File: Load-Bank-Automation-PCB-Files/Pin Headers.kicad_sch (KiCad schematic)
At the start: 23 parts, among them J10 Conn_01x04_Pin, J11 Conn_01x04_Pin, J12 Conn_01x04_Pin, J13 Conn_01x04_Pin, J14 Conn_01x04_Pin, J15 Conn_01x04_Pin, J16 Conn_01x04_Pin, J17 Conn_01x04_Pin, J18 Conn_01x04_Pin, J19 Conn_01x04_Pin, J20 Conn_01x04_Pin, J21 Conn_01x04_Pin, J22 Conn_01x04_Pin, J23 Conn_01x04_Pin, J4 Conn_01x04_Pin, J5 Conn_01x04_Pin, J6 Conn_01x04_Pin, J7 Conn_01x04_Pin, J8 Conn_01x04_Pin, J9 Conn_01x04_Pin, SW2 RESET, U9 STM32G491VETx

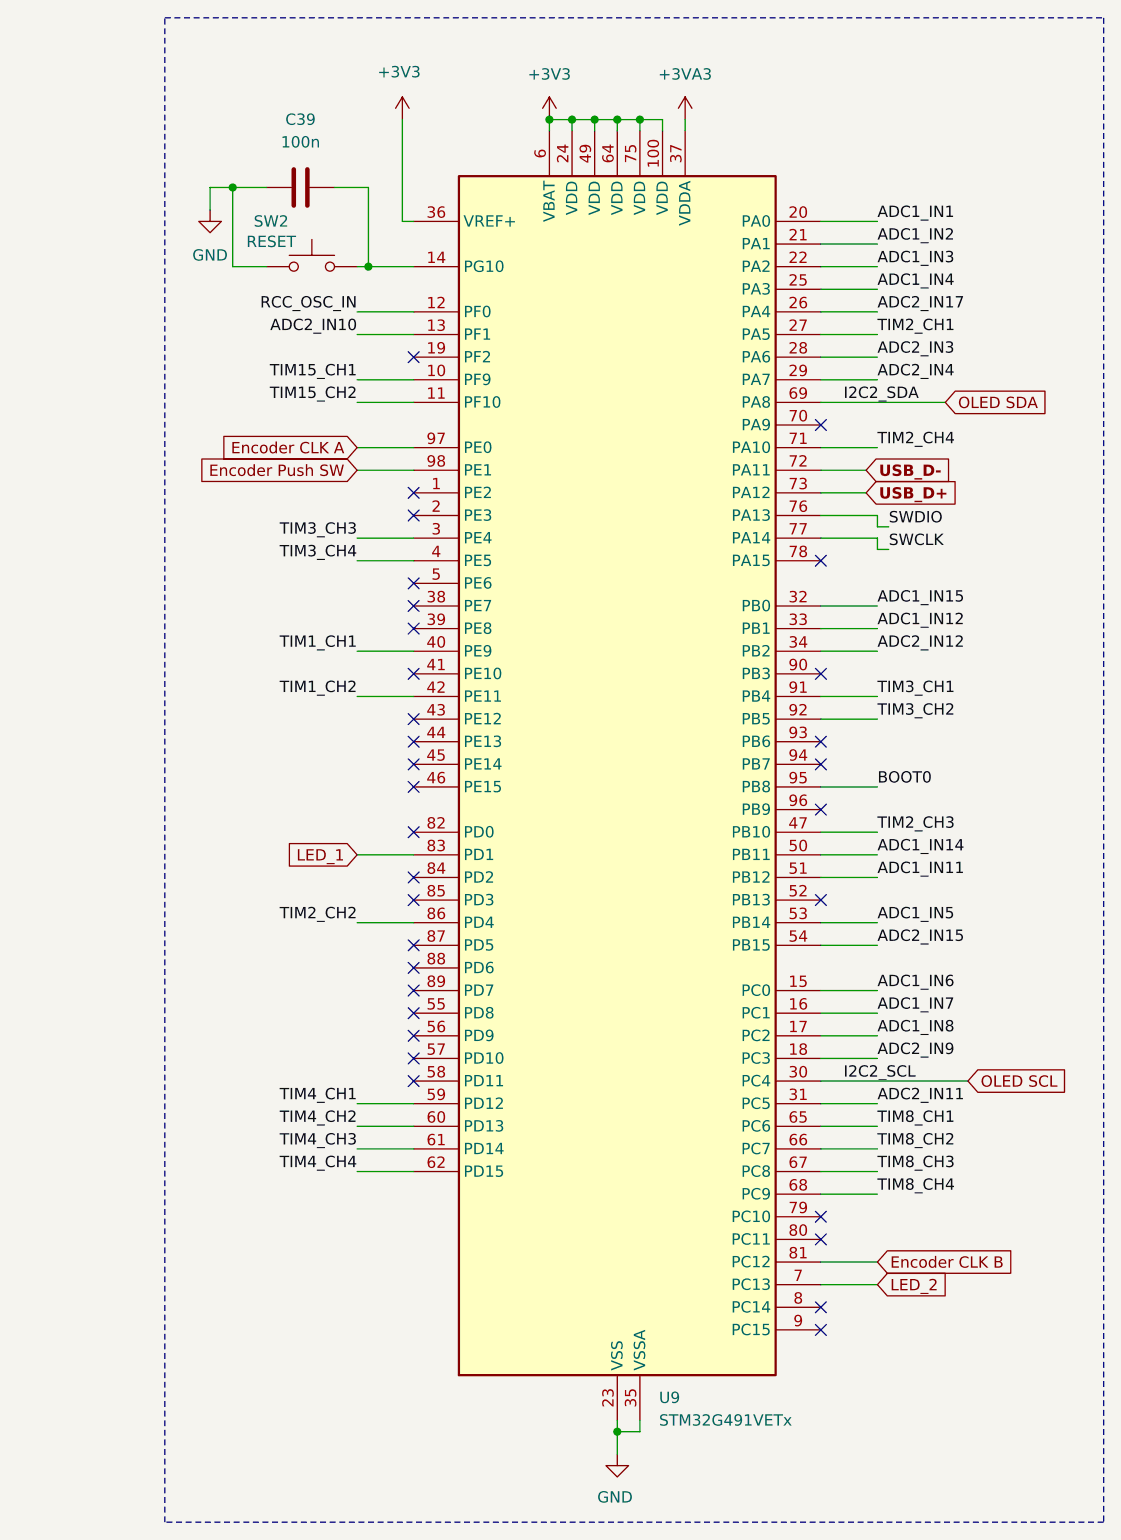
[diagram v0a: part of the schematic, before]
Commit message: Added potentiometer to buck converter and New schematic for MOSFET boards
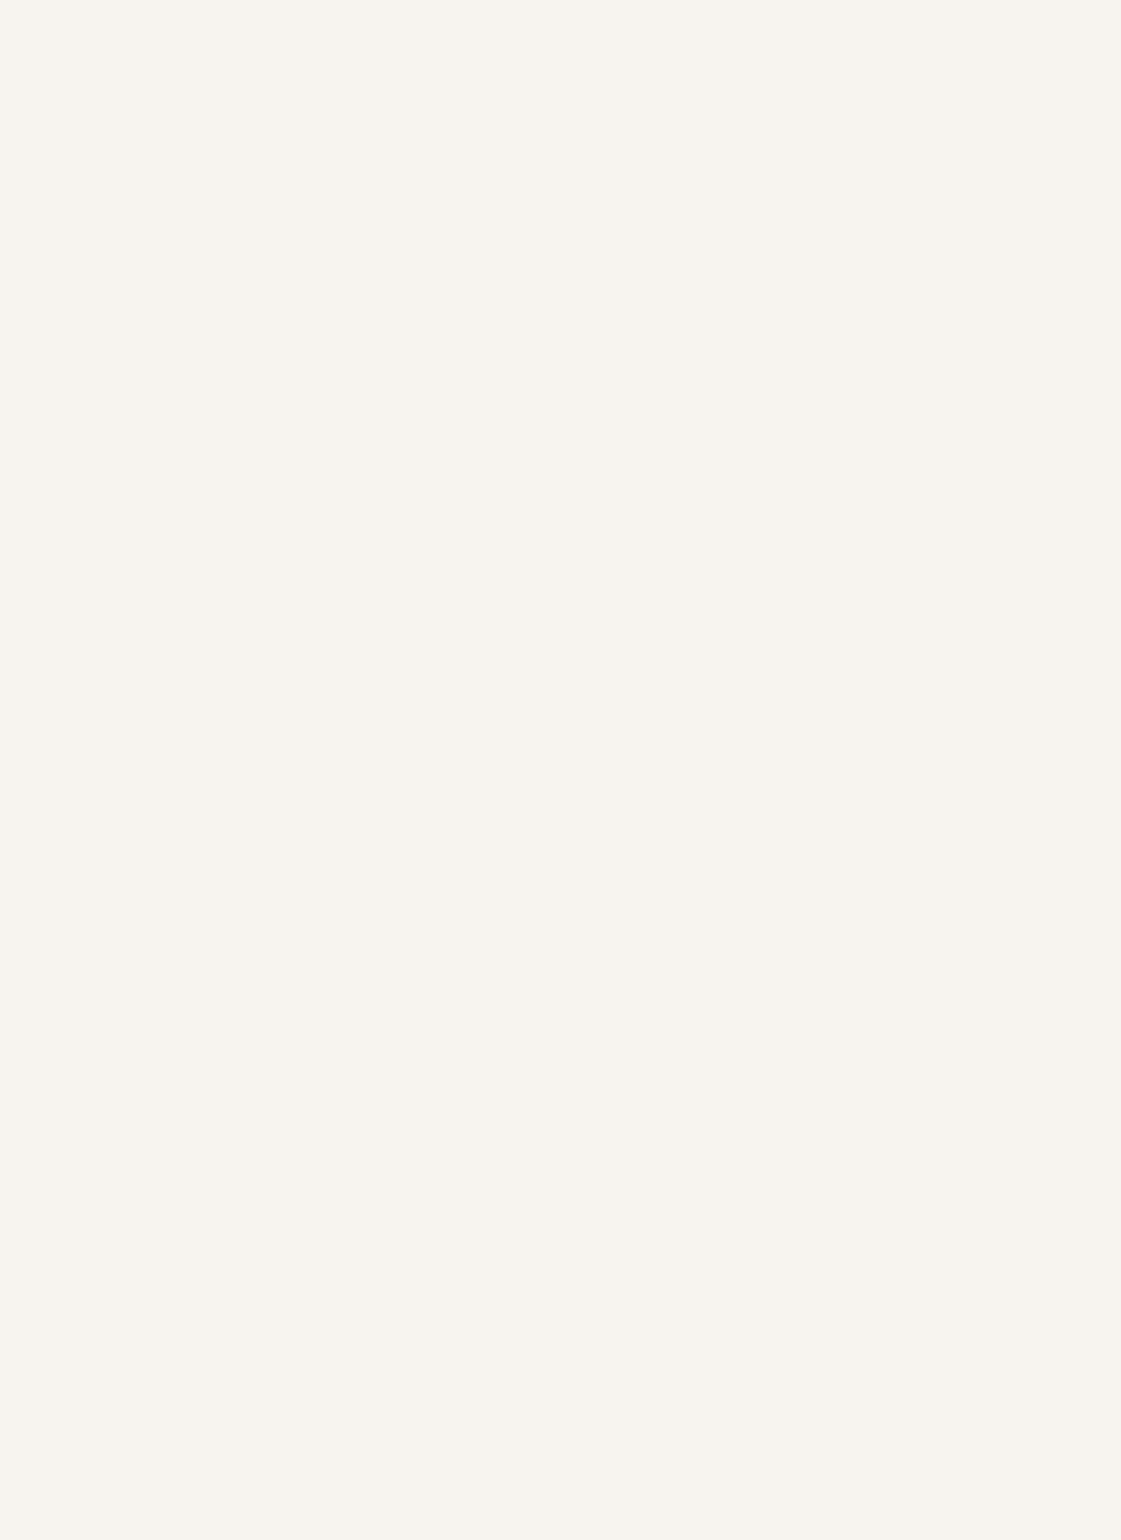
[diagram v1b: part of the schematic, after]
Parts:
- removed C39: 100n, symbol Device:C
- removed SW2: RESET, symbol Switch:SW_Push
- removed U9: STM32G491VETx, Package_QFP:LQFP-100_14x14mm_P0.5mm, symbol MCU_ST_STM32G4:STM32G491VETx
- J10, J11, J12, J13, J14, J15, J16, J17, J18, J19, J20, J21, J22, J23, J4, J5, J6, J7, J8, J9: footprint (none) -> Connector_PinHeader_2.54mm:PinHeader_1x04_P2.54mm_Vertical
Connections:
- no-connect marks 32 -> 0

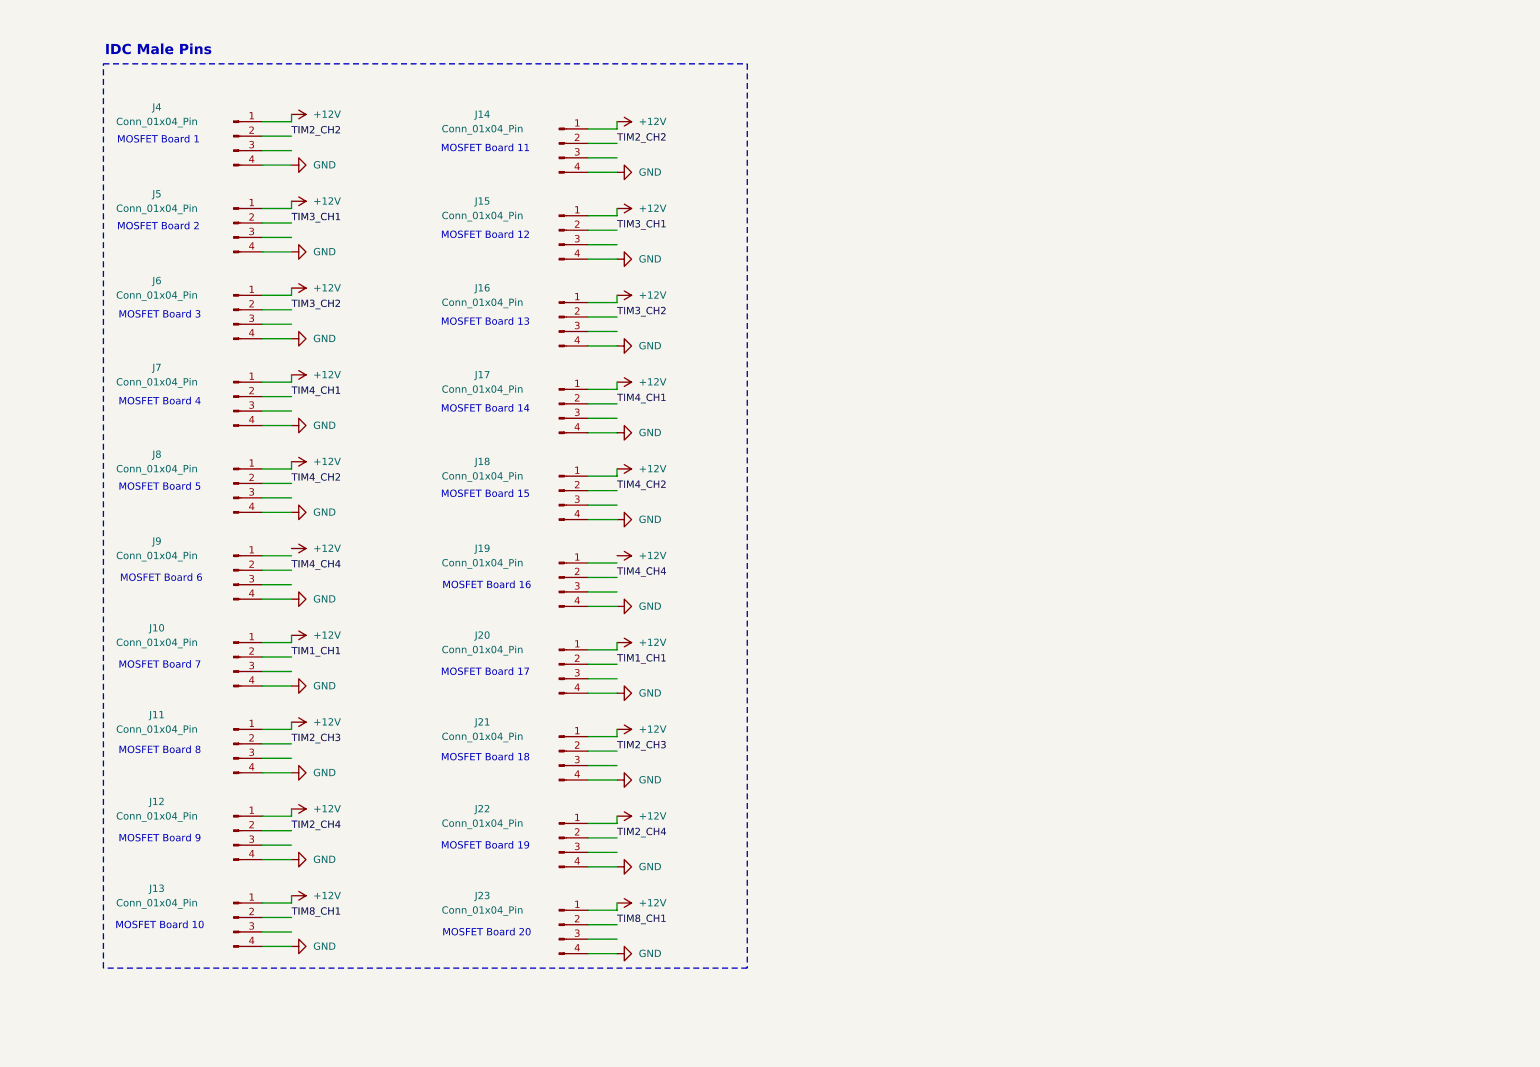
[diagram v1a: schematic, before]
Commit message: Comlpeted Schematic(needs some small component values only)
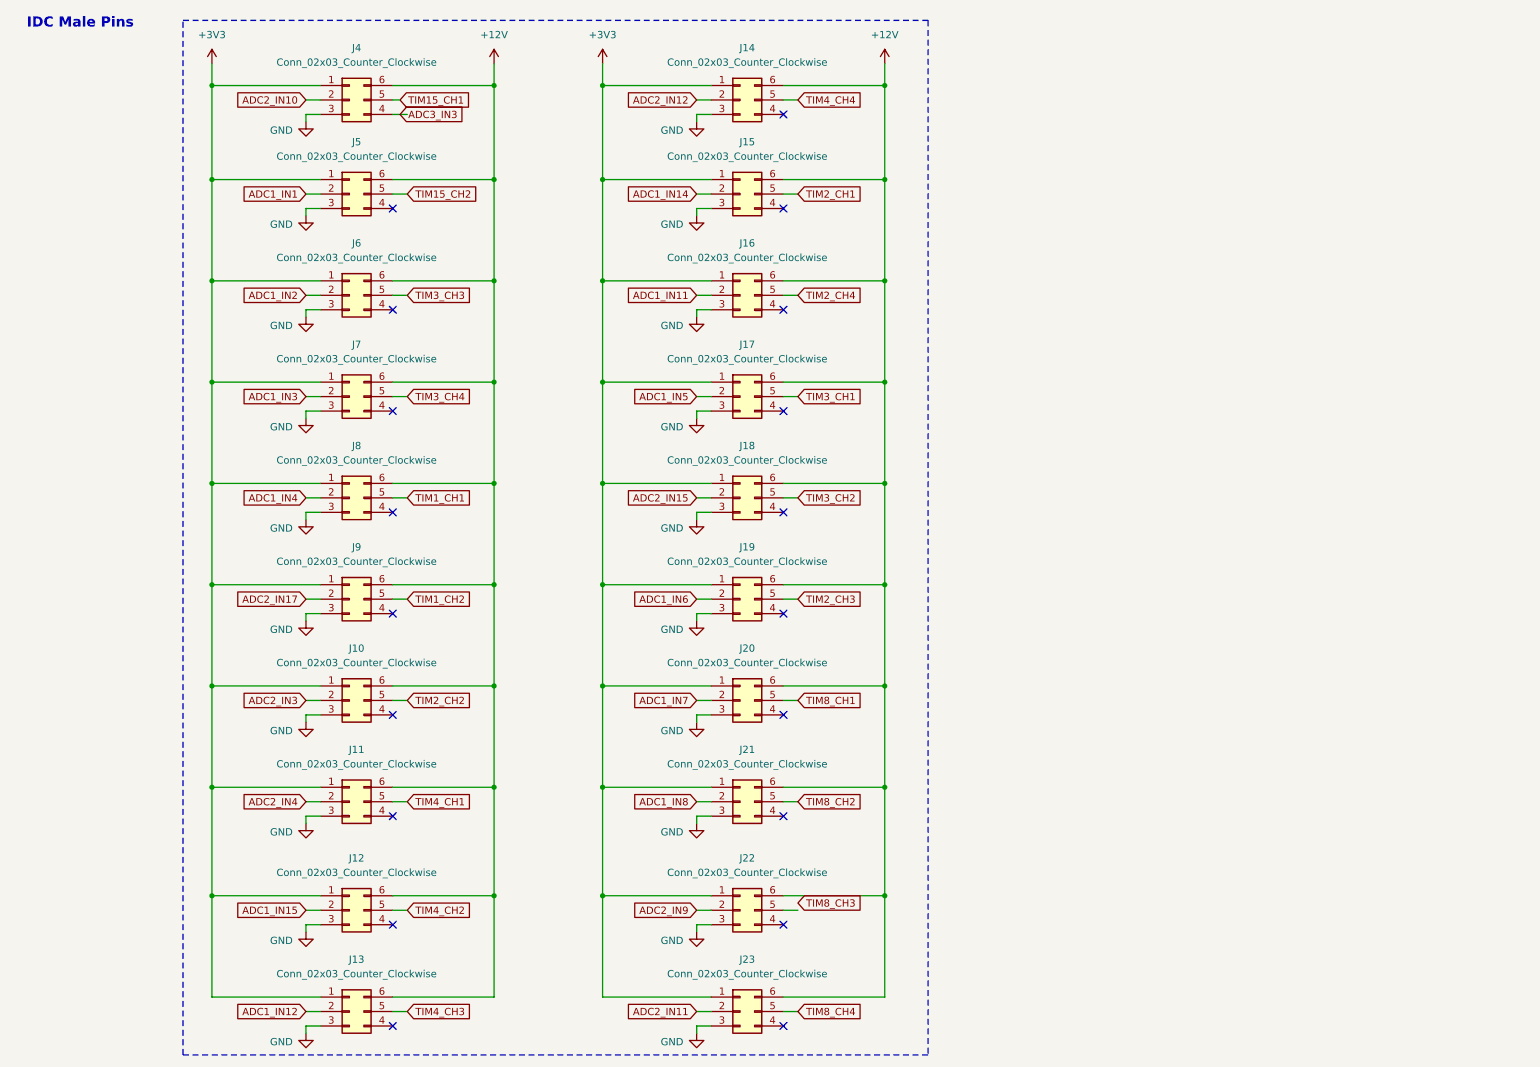
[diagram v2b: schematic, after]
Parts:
- removed J10, J11, J12, J13, J14, J15, J16, J17, J18, J19, J20, J21, J22, J23, J4, J5, J6, J7, J8, J9: Conn_01x04_Pin, Connector_PinHeader_2.54mm:PinHeader_1x04_P2.54mm_Vertical, symbol Connector:Conn_01x04_Pin
- added J10, J11, J12, J13, J14, J15, J16, J17, J18, J19, J20, J21, J22, J23, J4, J5, J6, J7, J8, J9: Conn_02x03_Counter_Clockwise, Connector_IDC:IDC-Header_2x03_P2.54mm_Vertical, symbol Connector_Generic:Conn_02x03_Counter_Clockwise
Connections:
- net +12V: now also J10.6 (Pin_6), J11.6 (Pin_6), J12.6 (Pin_6), J13.6 (Pin_6), J14.6 (Pin_6), J15.6 (Pin_6), J16.6 (Pin_6), J17.6 (Pin_6), J18.6 (Pin_6), J19.6 (Pin_6), J20.6 (Pin_6), J21.6 (Pin_6), J22.6 (Pin_6), J23.6 (Pin_6), J4.6 (Pin_6), J5.6 (Pin_6), J6.6 (Pin_6), J7.6 (Pin_6), J8.6 (Pin_6), J9.6 (Pin_6)
- net GND: now also J10.3 (Pin_3), J11.3 (Pin_3), J12.3 (Pin_3), J13.3 (Pin_3), J14.3 (Pin_3), J15.3 (Pin_3), J16.3 (Pin_3), J17.3 (Pin_3), J18.3 (Pin_3), J19.3 (Pin_3), J20.3 (Pin_3), J21.3 (Pin_3), J22.3 (Pin_3), J23.3 (Pin_3), J4.3 (Pin_3), J5.3 (Pin_3), J6.3 (Pin_3), J7.3 (Pin_3), J8.3 (Pin_3), J9.3 (Pin_3)
- net TIM1_CH1: now also J8.5 (Pin_5)
- net TIM2_CH2: now also J10.5 (Pin_5)
- net TIM2_CH3: now also J19.5 (Pin_5)
- net TIM2_CH4: now also J16.5 (Pin_5)
- net TIM3_CH1: now also J17.5 (Pin_5)
- net TIM3_CH2: now also J18.5 (Pin_5)
- net TIM4_CH1: now also J11.5 (Pin_5)
- net TIM4_CH2: now also J12.5 (Pin_5)
- net TIM4_CH4: now also J14.5 (Pin_5)
- net TIM8_CH1: now also J20.5 (Pin_5)
- new net +3V3: J10.1 (Pin_1), J11.1 (Pin_1), J12.1 (Pin_1), J13.1 (Pin_1), J14.1 (Pin_1), J15.1 (Pin_1), J16.1 (Pin_1), J17.1 (Pin_1), J18.1 (Pin_1), J19.1 (Pin_1), J20.1 (Pin_1), J21.1 (Pin_1), J22.1 (Pin_1), J23.1 (Pin_1), J4.1 (Pin_1), J5.1 (Pin_1), J6.1 (Pin_1), J7.1 (Pin_1), J8.1 (Pin_1), J9.1 (Pin_1)
- new net ADC1_IN1: J5.2 (Pin_2)
- new net ADC1_IN11: J16.2 (Pin_2)
- new net ADC1_IN12: J13.2 (Pin_2)
- new net ADC1_IN14: J15.2 (Pin_2)
- new net ADC1_IN15: J12.2 (Pin_2)
- new net ADC1_IN2: J6.2 (Pin_2)
- new net ADC1_IN3: J7.2 (Pin_2)
- new net ADC1_IN4: J8.2 (Pin_2)
- new net ADC1_IN5: J17.2 (Pin_2)
- new net ADC1_IN6: J19.2 (Pin_2)
- new net ADC1_IN7: J20.2 (Pin_2)
- new net ADC1_IN8: J21.2 (Pin_2)
- new net ADC2_IN10: J4.2 (Pin_2)
- new net ADC2_IN11: J23.2 (Pin_2)
- new net ADC2_IN12: J14.2 (Pin_2)
- new net ADC2_IN15: J18.2 (Pin_2)
- new net ADC2_IN17: J9.2 (Pin_2)
- new net ADC2_IN3: J10.2 (Pin_2)
- new net ADC2_IN4: J11.2 (Pin_2)
- new net ADC2_IN9: J22.2 (Pin_2)
- new net ADC3_IN3: J4.4 (Pin_4)
- new net TIM15_CH1: J4.5 (Pin_5)
- new net TIM15_CH2: J5.5 (Pin_5)
- new net TIM1_CH2: J9.5 (Pin_5)
- new net TIM2_CH1: J15.5 (Pin_5)
- new net TIM3_CH3: J6.5 (Pin_5)
- new net TIM3_CH4: J7.5 (Pin_5)
- new net TIM4_CH3: J13.5 (Pin_5)
- new net TIM8_CH2: J21.5 (Pin_5)
- new net TIM8_CH4: J23.5 (Pin_5)
- no-connect marks 0 -> 19
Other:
- note removed: "MOSFET Board 1"
- note removed: "MOSFET Board 10"
- note removed: "MOSFET Board 11"
- note removed: "MOSFET Board 12"
- note removed: "MOSFET Board 13"
- note removed: "MOSFET Board 14"
- note removed: "MOSFET Board 15"
- note removed: "MOSFET Board 16"
- note removed: "MOSFET Board 17"
- note removed: "MOSFET Board 18"
- note removed: "MOSFET Board 19"
- note removed: "MOSFET Board 2"
- note removed: "MOSFET Board 20"
- note removed: "MOSFET Board 3"
- note removed: "MOSFET Board 4"
- note removed: "MOSFET Board 5"
- note removed: "MOSFET Board 6"
- note removed: "MOSFET Board 7"
- note removed: "MOSFET Board 8"
- note removed: "MOSFET Board 9"
